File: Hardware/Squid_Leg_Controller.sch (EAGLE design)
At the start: 17 parts, among them IC1 REG1117, J1 SPI_PRG, X1 HEADER_POS3_70543, X2 HEADER_POS6_70543

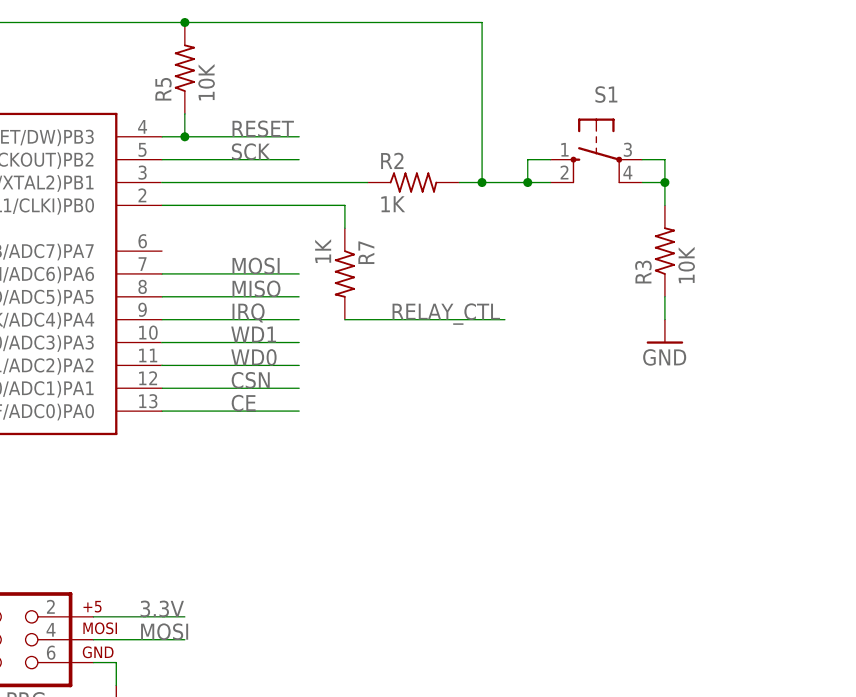
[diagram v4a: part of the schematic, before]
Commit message: slight adjustment to board, better silk screen, changed switch to locking connector, broke out extra IO, and moved mounting hole
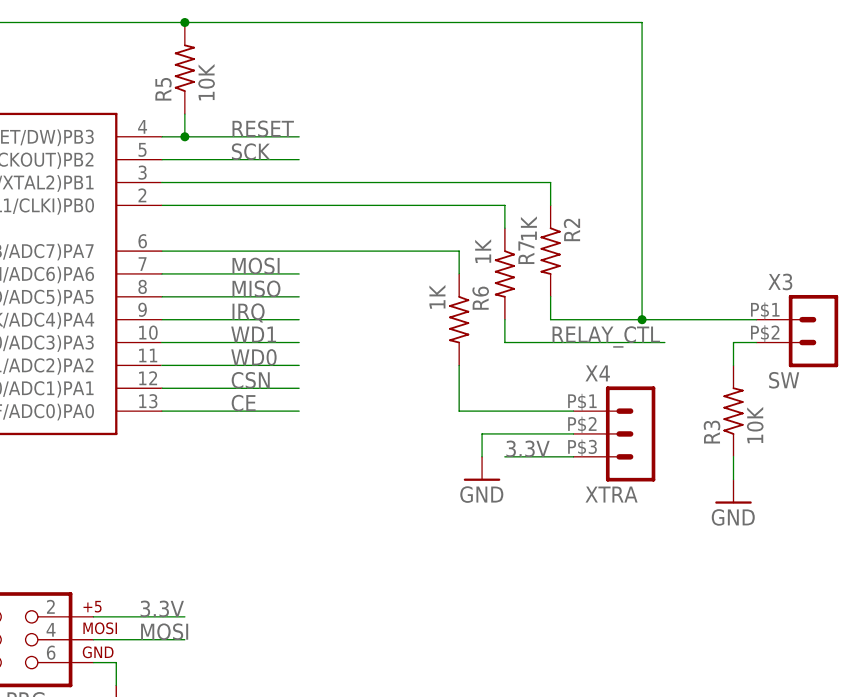
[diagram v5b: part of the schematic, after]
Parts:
- removed S1: (no value), switch-omron:10-XX
- added R6: 1K, resistor:R-US_R0603
- added X3: SW, Derp - Connectors - Molex SL:HEADER_POS2_70543
- added X4: XTRA, Derp - Connectors - Molex SL:HEADER_POS3_70543
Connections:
- new net N$3: R6.1, U$1.(PCINT7/ICP/OC0B/ADC7)PA7
- new net N$6: R6.2, X4.1
- net 3.3V: now also X3.1, X4.3; no longer S1.S, S1.S1
- net GND: now also X4.2
- net N$2: now also X3.2; no longer S1.P, S1.P1
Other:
- moved on the sheet: R2, R3, R7
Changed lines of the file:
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@@
 <part name="Q1" library="adafruit" deviceset="MOSFET-N" device="REFLOW"/>
 <part name="X2" library="Derp - Connectors - Molex SL" deviceset="HEADER_POS6_?" device="70543"/>
-<part name="S1" library="switch-omron" deviceset="10-XX" device=""/>
 <part name="R2" library="resistor" deviceset="R-US_" device="R0603" value="1K"/>
 <part name="R3" library="resistor" deviceset="R-US_" device="R0603" value="10K"/>
 <part name="GND5" library="supply1" deviceset="GND" device=""/>
+<part name="X3" library="Derp - Connectors - Molex SL" deviceset="HEADER_POS2_?" device="70543" value="SW"/>
+<part name="R6" library="resistor" deviceset="R-US_" device="R0603" value="1K"/>
+<part name="X4" library="Derp - Connectors - Molex SL" deviceset="HEADER_POS3_?" device="70543" value="XTRA"/>
+<part name="GND6" library="supply1" deviceset="GND" device=""/>
 </parts>
 <sheets>
@@
 <instance part="P+2" gate="VCC" x="25.4" y="25.4"/>
 <instance part="R5" gate="G$1" x="162.56" y="78.74" rot="R90"/>
-<instance part="R7" gate="G$1" x="180.34" y="55.88" rot="R270"/>
+<instance part="R7" gate="G$1" x="198.12" y="55.88" rot="R270"/>
 <instance part="D1" gate="D" x="5.08" y="60.96" rot="R90"/>
 <instance part="X1" gate="G$1" x="35.56" y="63.5"/>
 <instance part="Q1" gate="G$1" x="45.72" y="43.18" rot="MR0"/>
 <instance part="X2" gate="G$1" x="10.16" y="15.24" rot="MR0"/>
-<instance part="S1" gate="1" x="208.28" y="68.58" rot="MR270"/>
-<instance part="R2" gate="G$1" x="187.96" y="66.04"/>
-<instance part="R3" gate="G$1" x="215.9" y="58.42" rot="R90"/>
-<instance part="GND5" gate="1" x="215.9" y="48.26"/>
+<instance part="R2" gate="G$1" x="203.2" y="58.42" rot="R270"/>
+<instance part="R3" gate="G$1" x="223.52" y="40.64" rot="R90"/>
+<instance part="GND5" gate="1" x="223.52" y="30.48"/>
+<instance part="X3" gate="G$1" x="231.14" y="48.26"/>
+<instance part="R6" gate="G$1" x="193.04" y="50.8" rot="R270"/>
+<instance part="X4" gate="G$1" x="210.82" y="38.1"/>
+<instance part="GND6" gate="1" x="195.58" y="33.02"/>
 </instances>
 <busses>
@@
 <segment>
 <pinref part="R3" gate="G$1" pin="1"/>
-<wire x1="215.9" y1="53.34" x2="215.9" y2="50.8" width="0.1524" layer="91"/>
+<wire x1="223.52" y1="35.56" x2="223.52" y2="33.02" width="0.1524" layer="91"/>
 <pinref part="GND5" gate="1" pin="GND"/>
+</segment>
+<segment>
+<pinref part="X4" gate="G$1" pin="2"/>
+<wire x1="205.74" y1="38.1" x2="195.58" y2="38.1" width="0.1524" layer="91"/>
+<wire x1="195.58" y1="38.1" x2="195.58" y2="35.56" width="0.1524" layer="91"/>
+<pinref part="GND6" gate="1" pin="GND"/>
 </segment>
 </net>
@@
 <wire x1="162.56" y1="83.82" x2="91.44" y2="83.82" width="0.1524" layer="91"/>
 <wire x1="91.44" y1="83.82" x2="91.44" y2="71.12" width="0.1524" layer="91"/>
-<wire x1="162.56" y1="83.82" x2="195.58" y2="83.82" width="0.1524" layer="91"/>
-<wire x1="195.58" y1="83.82" x2="195.58" y2="66.04" width="0.1524" layer="91"/>
+<wire x1="162.56" y1="83.82" x2="213.36" y2="83.82" width="0.1524" layer="91"/>
+<wire x1="213.36" y1="83.82" x2="213.36" y2="50.8" width="0.1524" layer="91"/>
 <pinref part="R2" gate="G$1" pin="2"/>
-<wire x1="195.58" y1="66.04" x2="193.04" y2="66.04" width="0.1524" layer="91"/>
-<pinref part="S1" gate="1" pin="S1"/>
-<wire x1="195.58" y1="66.04" x2="200.66" y2="66.04" width="0.1524" layer="91"/>
-<junction x="195.58" y="66.04"/>
-<pinref part="S1" gate="1" pin="S"/>
-<wire x1="200.66" y1="66.04" x2="203.2" y2="66.04" width="0.1524" layer="91"/>
-<wire x1="203.2" y1="68.58" x2="200.66" y2="68.58" width="0.1524" layer="91"/>
-<wire x1="200.66" y1="68.58" x2="200.66" y2="66.04" width="0.1524" layer="91"/>
-<junction x="200.66" y="66.04"/>
+<wire x1="213.36" y1="50.8" x2="203.2" y2="50.8" width="0.1524" layer="91"/>
+<wire x1="203.2" y1="50.8" x2="203.2" y2="53.34" width="0.1524" layer="91"/>
+<junction x="213.36" y="50.8"/>
 <junction x="162.56" y="83.82"/>
+<pinref part="X3" gate="G$1" pin="1"/>
+<wire x1="213.36" y1="50.8" x2="226.06" y2="50.8" width="0.1524" layer="91"/>
 </segment>
 <segment>
@@
 <label x="157.48" y="17.78" size="1.778" layer="95"/>
 </segment>
+<segment>
+<pinref part="X4" gate="G$1" pin="3"/>
+<wire x1="205.74" y1="35.56" x2="198.12" y2="35.56" width="0.1524" layer="91"/>
+<label x="198.12" y="35.56" size="1.778" layer="95"/>
+</segment>
 </net>
 <net name="N$5" class="0">
@@
 <segment>
 <pinref part="R7" gate="G$1" pin="2"/>
-<wire x1="180.34" y1="50.8" x2="198.12" y2="50.8" width="0.1524" layer="91"/>
-<label x="185.42" y="50.8" size="1.778" layer="95"/>
+<wire x1="198.12" y1="50.8" x2="198.12" y2="48.26" width="0.1524" layer="91"/>
+<wire x1="198.12" y1="48.26" x2="215.9" y2="48.26" width="0.1524" layer="91"/>
+<label x="203.2" y="48.26" size="1.778" layer="95"/>
 </segment>
 </net>
@@
 <pinref part="U$1" gate="G$1" pin="(PCINT8/XTAL1/CLKI)PB0"/>
 <pinref part="R7" gate="G$1" pin="1"/>
-<wire x1="160.02" y1="63.5" x2="180.34" y2="63.5" width="0.1524" layer="91"/>
-<wire x1="180.34" y1="63.5" x2="180.34" y2="60.96" width="0.1524" layer="91"/>
+<wire x1="160.02" y1="63.5" x2="198.12" y2="63.5" width="0.1524" layer="91"/>
+<wire x1="198.12" y1="63.5" x2="198.12" y2="60.96" width="0.1524" layer="91"/>
 </segment>
 </net>
@@
 <pinref part="U$1" gate="G$1" pin="(PCINT9/XTAL2)PB1"/>
 <pinref part="R2" gate="G$1" pin="1"/>
-<wire x1="160.02" y1="66.04" x2="182.88" y2="66.04" width="0.1524" layer="91"/>
+<wire x1="160.02" y1="66.04" x2="203.2" y2="66.04" width="0.1524" layer="91"/>
+<wire x1="203.2" y1="66.04" x2="203.2" y2="63.5" width="0.1524" layer="91"/>
 </segment>
 </net>
 <net name="N$2" class="0">
 <segment>
-<pinref part="S1" gate="1" pin="P1"/>
-<wire x1="215.9" y1="66.04" x2="213.36" y2="66.04" width="0.1524" layer="91"/>
 <pinref part="R3" gate="G$1" pin="2"/>
-<wire x1="215.9" y1="66.04" x2="215.9" y2="63.5" width="0.1524" layer="91"/>
-<pinref part="S1" gate="1" pin="P"/>
-<wire x1="213.36" y1="68.58" x2="215.9" y2="68.58" width="0.1524" layer="91"/>
-<wire x1="215.9" y1="68.58" x2="215.9" y2="66.04" width="0.1524" layer="91"/>
-<junction x="215.9" y="66.04"/>
-</segment>
-</net>
+<wire x1="223.52" y1="48.26" x2="223.52" y2="45.72" width="0.1524" layer="91"/>
+<pinref part="X3" gate="G$1" pin="2"/>
+<wire x1="226.06" y1="48.26" x2="223.52" y2="48.26" width="0.1524" layer="91"/>
+</segment>
+</net>
+<net name="N$3" class="0">
+<segment>
+<pinref part="U$1" gate="G$1" pin="(PCINT7/ICP/OC0B/ADC7)PA7"/>
+<pinref part="R6" gate="G$1" pin="1"/>
+<wire x1="160.02" y1="58.42" x2="193.04" y2="58.42" width="0.1524" layer="91"/>
+<wire x1="193.04" y1="58.42" x2="193.04" y2="55.88" width="0.1524" layer="91"/>
+</segment>
+</net>
+<net name="N$6" class="0">
+<segment>
+<pinref part="R6" gate="G$1" pin="2"/>
+<wire x1="193.04" y1="45.72" x2="193.04" y2="40.64" width="0.1524" layer="91"/>
+<pinref part="X4" gate="G$1" pin="1"/>
+<wire x1="193.04" y1="40.64" x2="205.74" y2="40.64" width="0.1524" layer="91"/>
+</segment>
+</net>
